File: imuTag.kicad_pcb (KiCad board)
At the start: 4 copper layers, 41.3 x 40 mm, 45 parts, among them J1 Conn_02x05_Odd_Even, J2 Conn_01x05_Socket, J3 Conn_01x02_Pin, Q1 DMG2305UX-13, U1 E73-2G4M08S1C, U2 ME6211C30M5G-N, U3 GD25Q64ESIG, U4 LSM6DSV16XTR, U5 LIS2MDLTR, Y2 Crystal

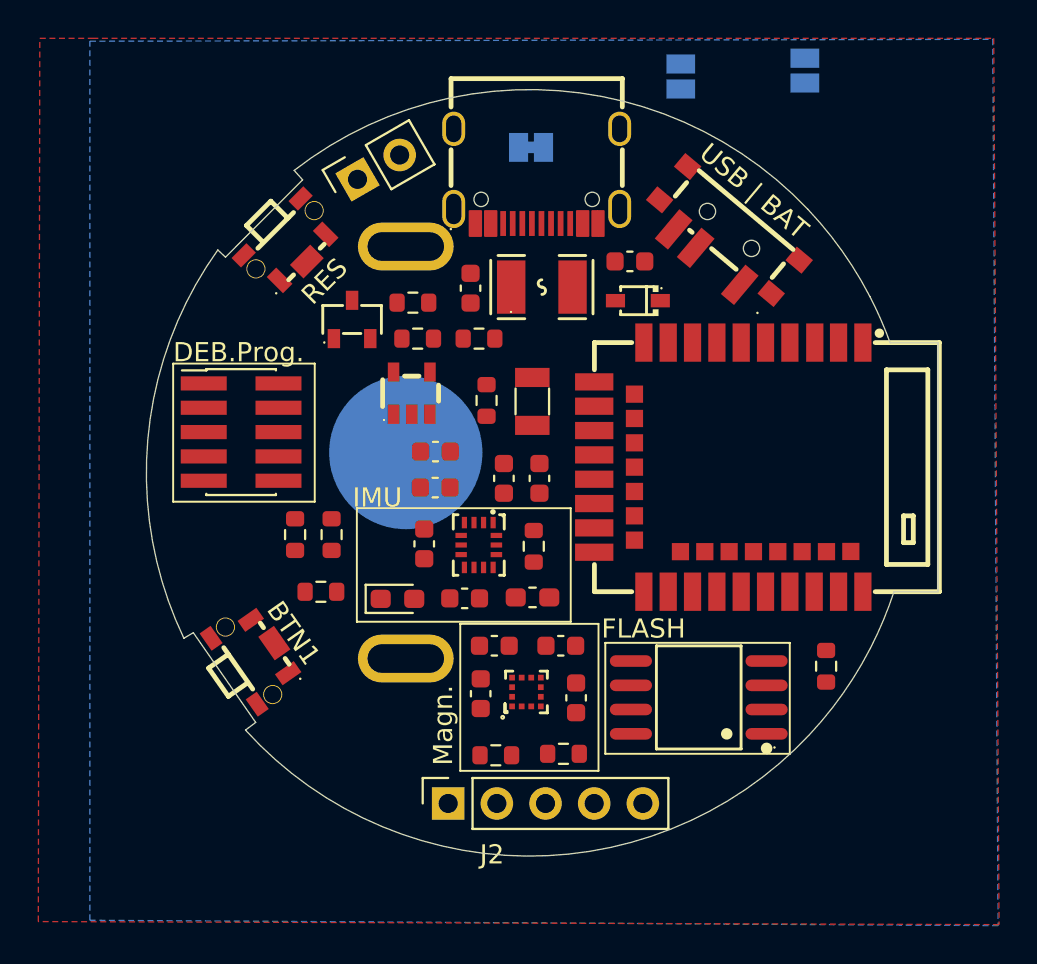
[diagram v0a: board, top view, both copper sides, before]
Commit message: Routing of critical Paths, Finalizing Zones
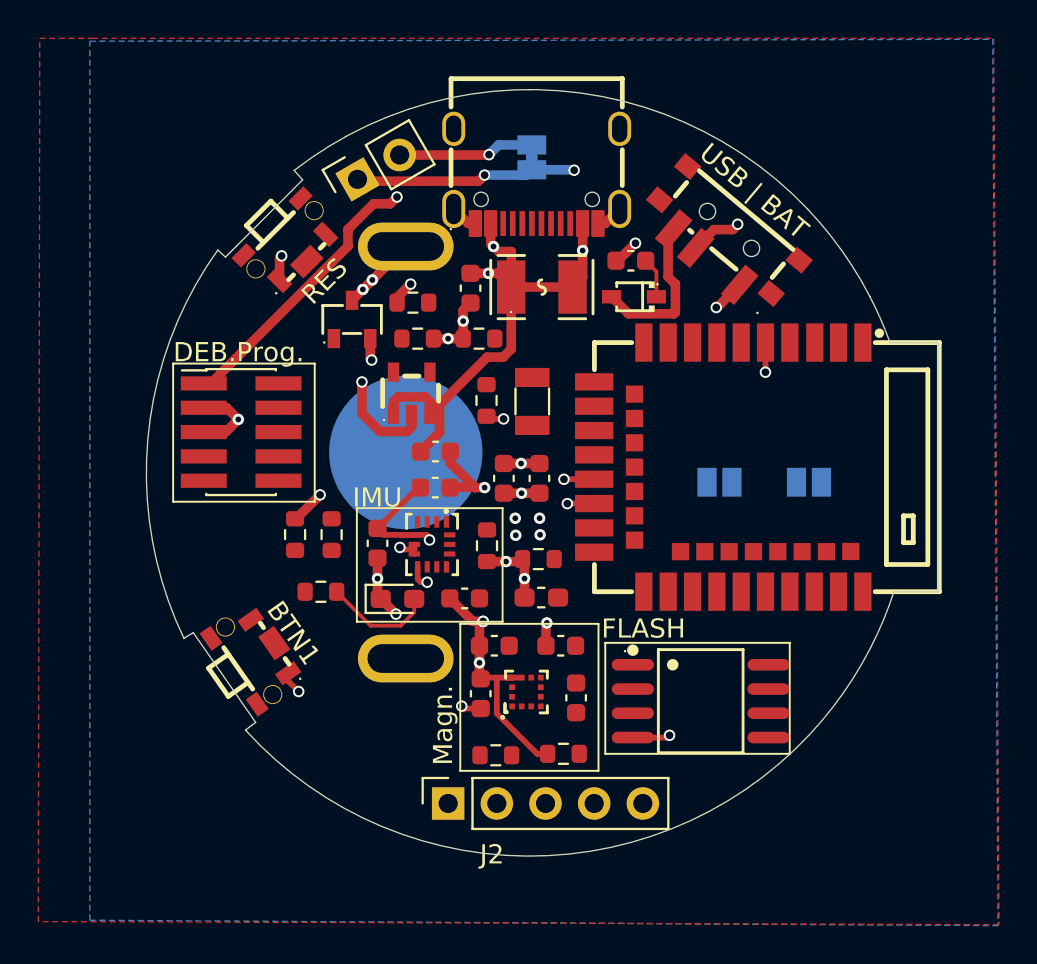
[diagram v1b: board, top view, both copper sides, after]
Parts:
- moved JP7 22.2 mm to (184.1, 100.6), turned to 180 degrees
- moved JP1 21.9 mm to (179.4, 100.6), turned to 180 degrees
- moved R11 16.0 mm to (169.9, 104.6), turned to 0 degrees
- moved C18 2.44 mm to (161.5, 103.8)
- moved R10 2.44 mm to (167.3, 103.9)
- moved U4 2.44 mm to (164.4, 103.9)
- moved JP2 0.52 mm to (169.6, 83.7), turned to -90 degrees
- moved L1 0.46 mm to (170.1, 106.6)
- moved D3 0.29 mm to (174.9, 90.9)
- moved U3 0.22 mm to (178.4, 112.0), turned to -90 degrees
- moved C3 0.06 mm to (174.8, 89.1)
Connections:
- U1 pad 16: /LIS2MDL_INT -> /LSM6DSV16_INT2
- U1 pad 17: unconnected-(U1-P1.09-Pad17) -> /LSM6DSV16_INT2
- U1 pad 38: /LSM6DSV16_INT2 -> /LIS2MDL_INT
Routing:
- net VCC: track 0.00 -> 55.0 mm, vias 0 -> 17
- net GND: track 0.00 -> 37.8 mm, vias 0 -> 17
- net /+5V_USB: track 0.00 -> 28.1 mm, vias 0 -> 3
- net /VCC_1: track 0.00 -> 24.9 mm, vias 0 -> 3
- net /VBAT1: track 0.00 -> 22.0 mm, vias 0 -> 2
- net /USB_3V0: track 0.00 -> 9.07 mm
- net /VBAT: track 0.00 -> 5.79 mm, vias 0 -> 3
- net Net-(D2-A): track 0.00 -> 5.76 mm
- net Net-(D3-K): track 0.00 -> 2.11 mm
- added copper zone on In2.Cu, net /+5V_USB
- added copper zone on In2.Cu, net /VBAT
- added copper zone on In1.Cu, net GND
- added copper zone on In2.Cu, net VCC
- removed copper zone on In1.Cu, net VCC

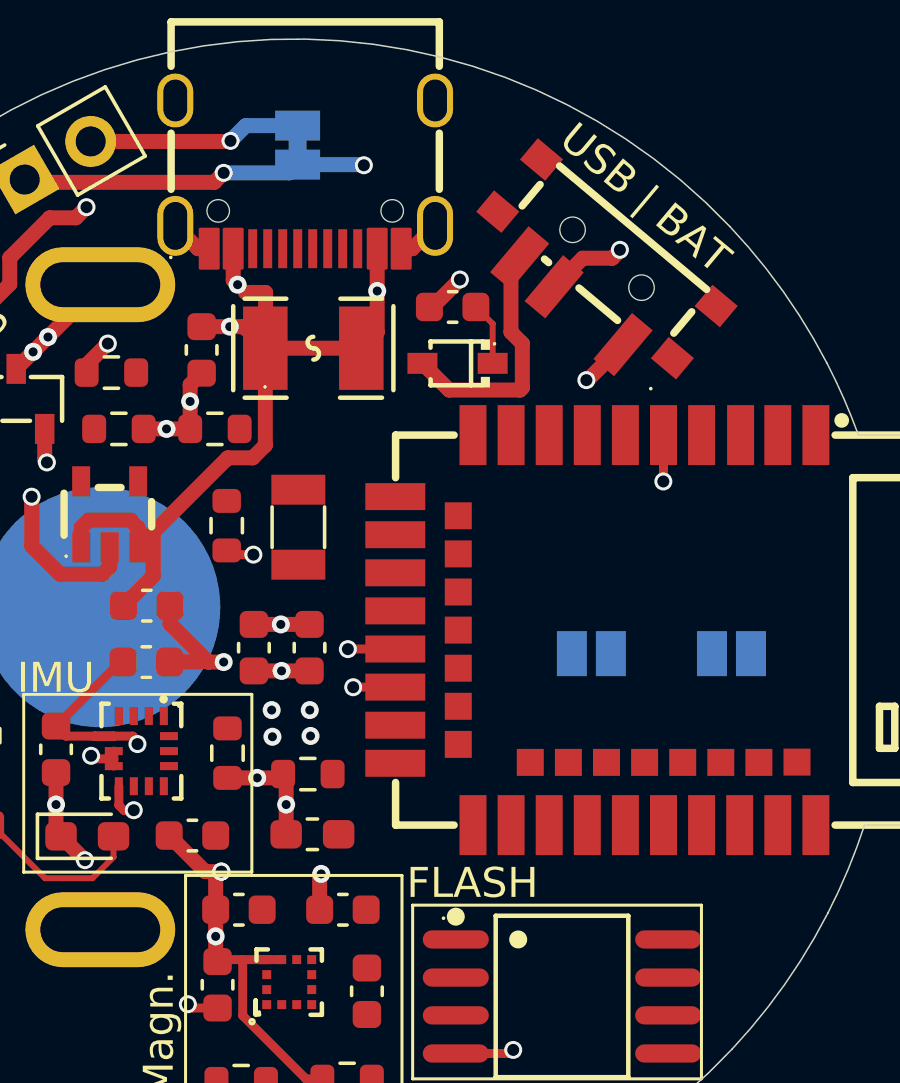
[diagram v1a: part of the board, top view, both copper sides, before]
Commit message: Route critical nets and finalize zones
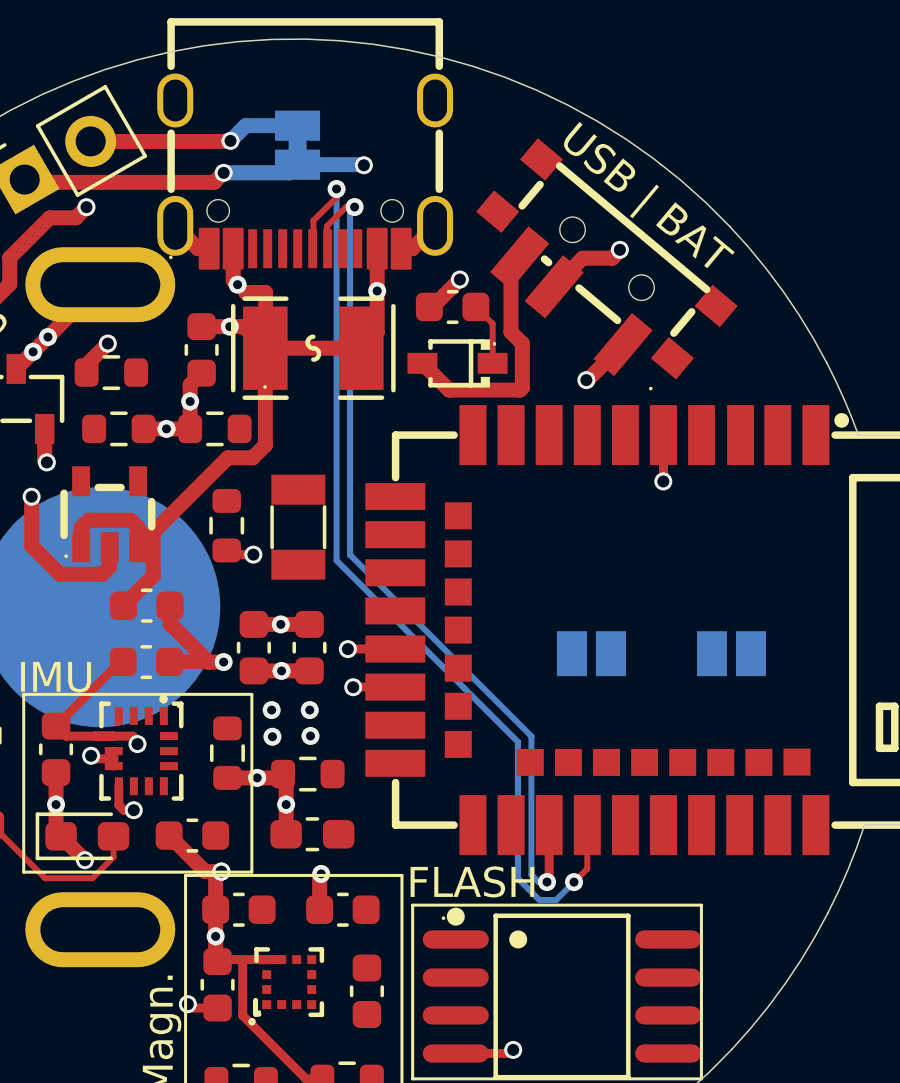
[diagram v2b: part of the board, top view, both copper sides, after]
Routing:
- net /USB_D+: track 0.00 -> 32.3 mm, vias 0 -> 2
- net /USB_D-: track 0.00 -> 29.3 mm, vias 0 -> 2
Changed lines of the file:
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@@
 		(net 26)
+	)
+	(segment
+		(start 170.5748 86.584256)
+		(end 170.5748 86.359599)
+		(width 0.2)
+		(layer "F.Cu")
+		(net 38)
+	)
+	(segment
+		(start 170.5998 87.109256)
+		(end 170.5998 86.609256)
+		(width 0.2)
+		(layer "F.Cu")
+		(net 38)
+	)
+	(segment
+		(start 177.982999 108.148001)
+		(end 177.982999 106.323148)
+		(width 0.3)
+		(layer "F.Cu")
+		(net 38)
+	)
+	(segment
+		(start 170.5998 86.609256)
+		(end 170.5748 86.584256)
+		(width 0.2)
+		(layer "F.Cu")
+		(net 38)
+	)
+	(segment
+		(start 177.909932 108.221068)
+		(end 177.982999 108.148001)
+		(width 0.3)
+		(layer "F.Cu")
+		(net 38)
+	)
+	(segment
+		(start 171.213678 85.720721)
+		(end 171.496521 85.720721)
+		(width 0.2)
+		(layer "F.Cu")
+		(net 38)
+	)
+	(segment
+		(start 170.5748 86.359599)
+		(end 171.213678 85.720721)
+		(width 0.2)
+		(layer "F.Cu")
+		(net 38)
+	)
+	(via
+		(at 171.496521 85.720721)
+		(size 0.6)
+		(drill 0.3)
+		(layers "F.Cu" "B.Cu")
+		(net 38)
+	)
+	(via
+		(at 177.909932 108.221068)
+		(size 0.6)
+		(drill 0.3)
+		(layers "F.Cu" "B.Cu")
+		(net 38)
+	)
+	(segment
+		(start 177.909932 108.221068)
+		(end 177.628503 108.221068)
+		(width 0.2)
+		(layer "B.Cu")
+		(net 38)
+	)
+	(segment
+		(start 177.39 107.982565)
+		(end 177.39 103.361002)
+		(width 0.2)
+		(layer "B.Cu")
+		(net 38)
+	)
+	(segment
+		(start 171.34548 97.316482)
+		(end 171.34548 85.871762)
+		(width 0.2)
+		(layer "B.Cu")
+		(net 38)
+	)
+	(segment
+		(start 177.628503 108.221068)
+		(end 177.39 107.982565)
+		(width 0.2)
+		(layer "B.Cu")
+		(net 38)
+	)
+	(segment
+		(start 171.34548 85.871762)
+		(end 171.496521 85.720721)
+		(width 0.2)
+		(layer "B.Cu")
+		(net 38)
+	)
+	(segment
+		(start 177.39 103.361002)
+		(end 171.34548 97.316482)
+		(width 0.2)
+		(layer "B.Cu")
+		(net 38)
+	)
+	(segment
+		(start 170.895479 85.402522)
+		(end 170.895479 85.119679)
+		(width 0.2)
+		(layer "F.Cu")
+		(net 55)
+	)
+	(segment
+		(start 170.1248 86.173201)
+		(end 170.895479 85.402522)
+		(width 0.2)
+		(layer "F.Cu")
+		(net 55)
+	)
+	(segment
+		(start 170.0998 87.109256)
+		(end 170.0998 86.609256)
+		(width 0.2)
+		(layer "F.Cu")
+		(net 55)
+	)
+	(segment
+		(start 178.810211 108.223611)
+		(end 179.252999 107.780824)
+		(width 0.2)
+		(layer "F.Cu")
+		(net 55)
+	)
+	(segment
+		(start 179.252999 107.780824)
+		(end 179.252999 106.323148)
+		(width 0.2)
+		(layer "F.Cu")
+		(net 55)
+	)
+	(segment
+		(start 170.1248 86.584256)
+		(end 170.1248 86.173201)
+		(width 0.2)
+		(layer "F.Cu")
+		(net 55)
+	)
+	(segment
+		(start 170.0998 86.609256)
+		(end 170.1248 86.584256)
+		(width 0.2)
+		(layer "F.Cu")
+		(net 55)
+	)
+	(via
+		(at 178.810211 108.223611)
+		(size 0.6)
+		(drill 0.3)
+		(layers "F.Cu" "B.Cu")
+		(net 55)
+	)
+	(via
+		(at 170.895479 85.119679)
+		(size 0.6)
+		(drill 0.3)
+		(layers "F.Cu" "B.Cu")
+		(net 55)
+	)
+	(segment
+		(start 176.94 108.099665)
+		(end 176.94 103.547398)
+		(width 0.2)
+		(layer "B.Cu")
+		(net 55)
+	)
+	(segment
+		(start 176.94 103.547398)
+		(end 170.895479 97.502877)
+		(width 0.2)
+		(layer "B.Cu")
+		(net 55)
+	)
+	(segment
+		(start 178.211755 108.822068)
+		(end 177.660989 108.822068)
+		(width 0.2)
+		(layer "B.Cu")
+		(net 55)
+	)
+	(segment
+		(start 170.895479 97.502877)
+		(end 170.895479 85.119679)
+		(width 0.2)
+		(layer "B.Cu")
+		(net 55)
+	)
+	(segment
+		(start 177.660989 108.822068)
+		(end 177.308932 108.470011)
+		(width 0.2)
+		(layer "B.Cu")
+		(net 55)
+	)
+	(segment
+		(start 178.810211 108.223611)
+		(end 178.211755 108.822068)
+		(width 0.2)
+		(layer "B.Cu")
+		(net 55)
+	)
+	(segment
+		(start 177.308932 108.470011)
+		(end 177.308932 108.468597)
+		(width 0.2)
+		(layer "B.Cu")
+		(net 55)
+	)
+	(segment
+		(start 177.308932 108.468597)
+		(end 176.94 108.099665)
+		(width 0.2)
+		(layer "B.Cu")
+		(net 55)
 	)
 	(zone

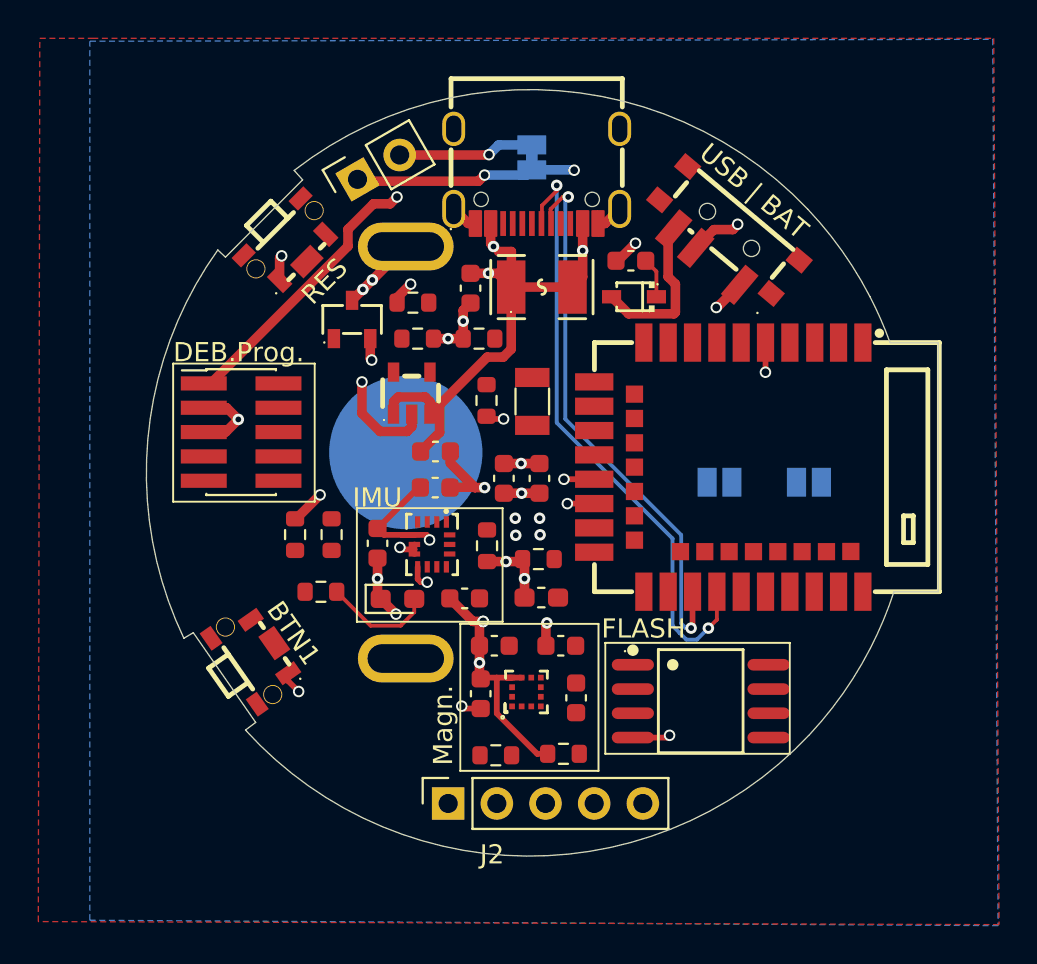
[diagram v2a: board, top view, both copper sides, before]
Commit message: Save current QSPI routing cleanup
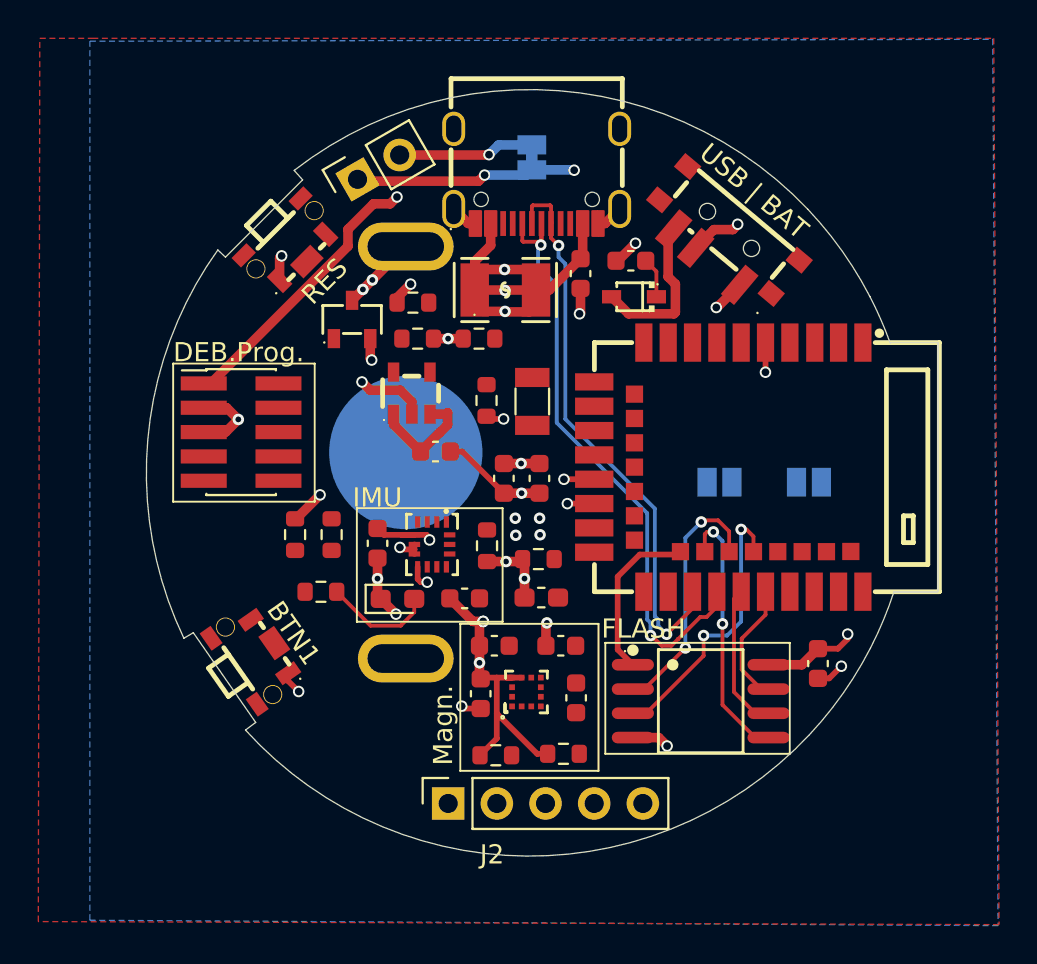
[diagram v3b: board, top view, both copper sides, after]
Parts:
- moved C14 22.0 mm to (184.5, 110.1), turned to 90 degrees
- moved C1 5.79 mm to (172.1, 89.7)
- moved F1 1.91 mm to (168.2, 90.6)
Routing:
- net /QSPI_IO2: track 0.00 -> 14.6 mm, vias 0 -> 2
- net /QSPI_IO0: track 0.00 -> 13.7 mm, vias 0 -> 2
- net /QSPI_IO1: track 0.00 -> 13.3 mm, vias 0 -> 2
- net /QSPI_CS: track 0.00 -> 8.74 mm
- net /QSPI_CLK: track 0.00 -> 7.65 mm
- net /QSPI_IO3: track 0.00 -> 6.40 mm
- net VCC: track 55.0 -> 59.4 mm, vias 17 -> 18
- net GND: track 37.8 -> 36.4 mm

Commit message: finalize power routing and decoupling capacitors
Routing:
- net Net-(D3-K): track 2.11 -> 18.6 mm, vias 0 -> 2
- net VCC: track 59.4 -> 70.7 mm, vias 18 -> 20
- net /+5V_USB: track 27.9 -> 36.8 mm
- net Net-(U1-XL2): track 0.00 -> 3.65 mm
- net Net-(U1-XL1): track 0.00 -> 3.33 mm
